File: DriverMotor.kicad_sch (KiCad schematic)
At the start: 15 parts, among them U3 DRV8874PWPR

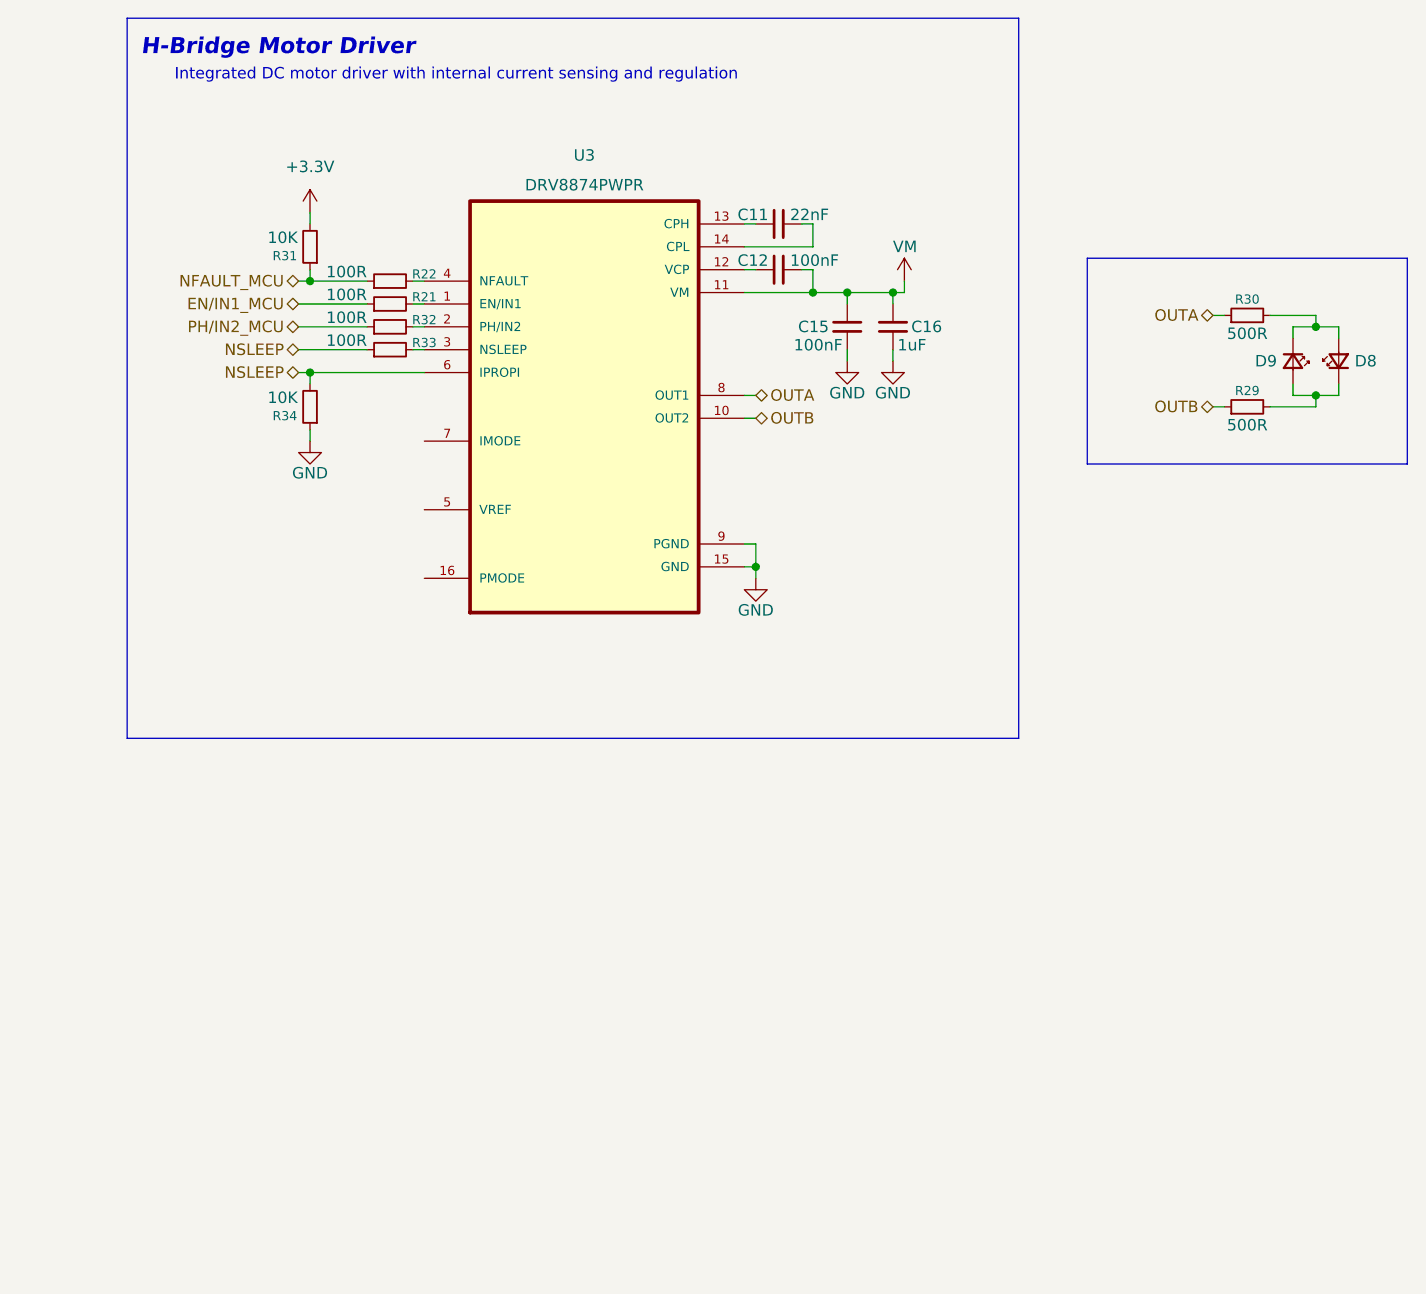
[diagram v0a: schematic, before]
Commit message: feat: integrate DRV8874 H-bridge stage with current sensing and polarity LEDs
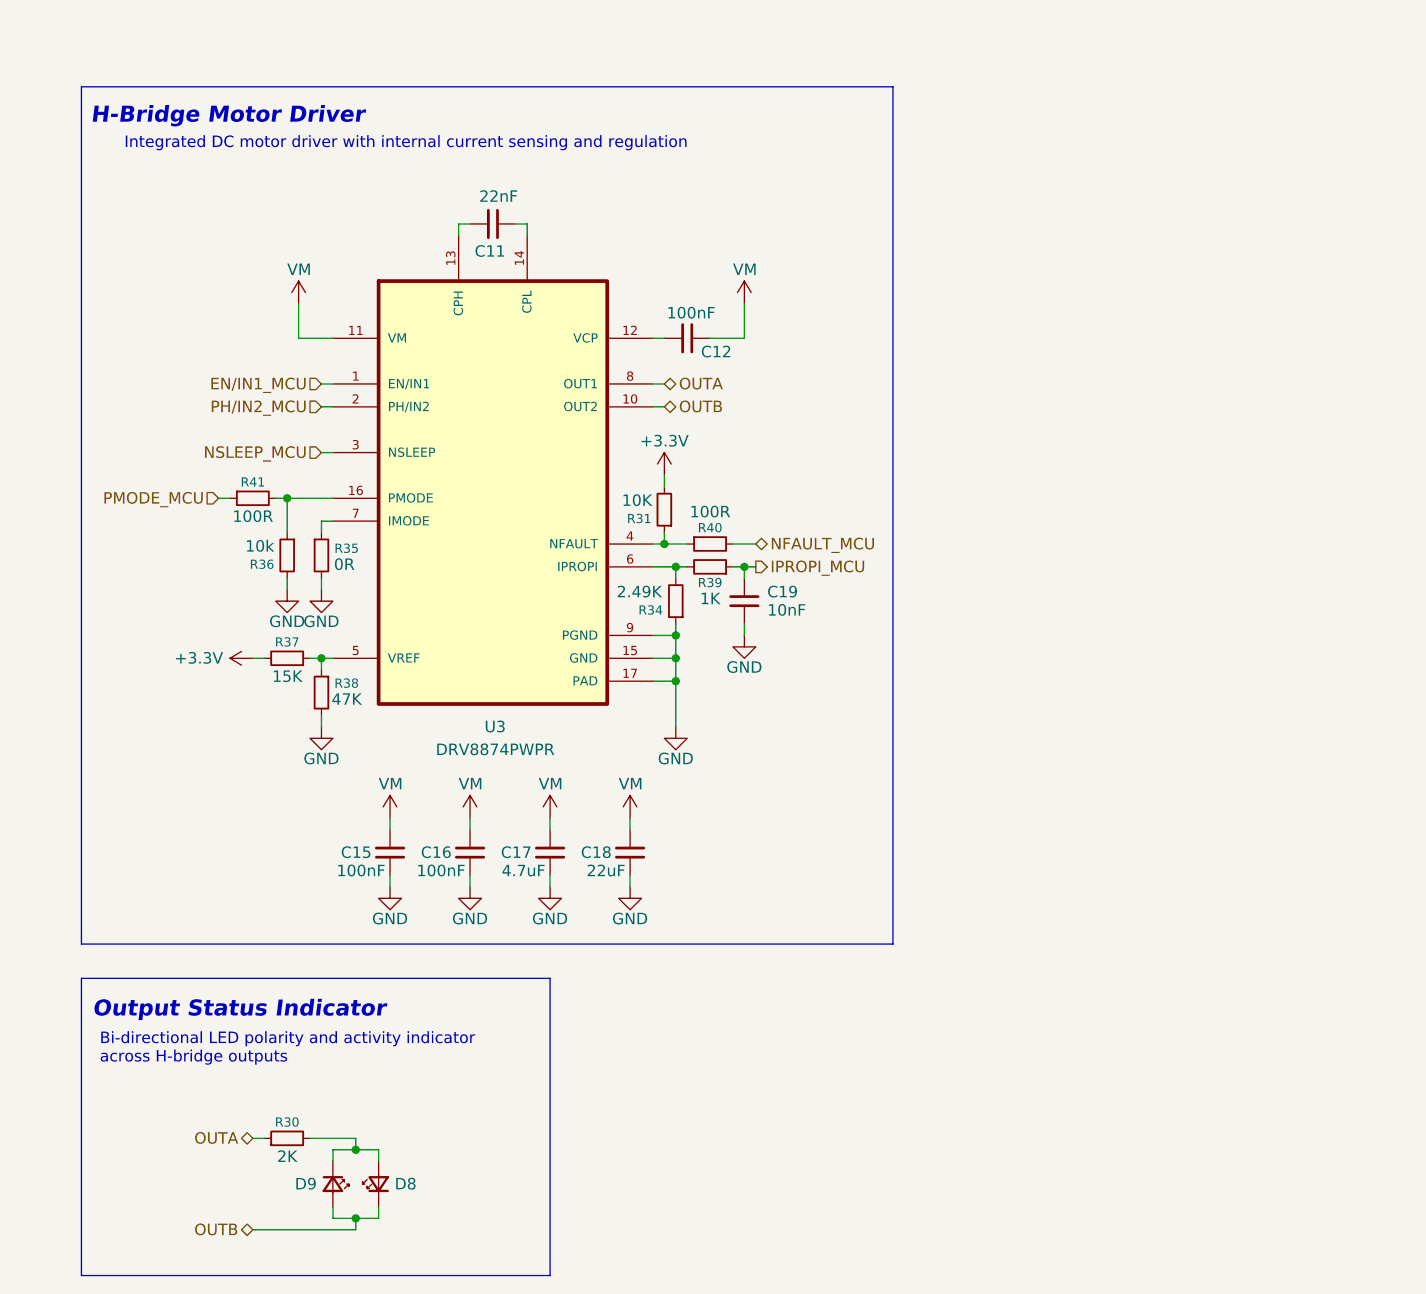
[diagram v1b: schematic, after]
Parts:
- removed R21, R22, R32, R33: 100R, Resistor_SMD:R_0603_1608Metric, symbol Device:R_Small
- removed R29: 500R, Resistor_SMD:R_0603_1608Metric, symbol Device:R_Small
- added C17: 4.7uF, Capacitor_SMD:C_0603_1608Metric, symbol Device:C_Small
- added C18: 22uF, Capacitor_SMD:C_0603_1608Metric, symbol Device:C_Small
- added C19: 10nF, Capacitor_SMD:C_0603_1608Metric, symbol Device:C_Small
- added R35: 0R, Resistor_SMD:R_0603_1608Metric, symbol Device:R_Small
- added R36: 10k, Resistor_SMD:R_0603_1608Metric, symbol Device:R_Small
- added R37: 15K, Resistor_SMD:R_0603_1608Metric, symbol Device:R_Small
- added R38: 47K, Resistor_SMD:R_0603_1608Metric, symbol Device:R_Small
- added R39: 1K, Resistor_SMD:R_0603_1608Metric, symbol Device:R_Small
- added R40, R41: 100R, Resistor_SMD:R_0603_1608Metric, symbol Device:R_Small
- C16: value 1uF -> 100nF
- R30: value 500R -> 2K
- R34: value 10K -> 2.49K
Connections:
- net +3.3V: now also R37.2
- net EN/IN1_MCU: now also U3.1 (EN/IN1)
- net GND: now also U3.17 (PAD), C17.2, C18.2, C19.1, R35.2, R36.2, R38.2
- net NFAULT_MCU: now also R40.2; no longer R31.1
- net OUTB: now also D8.1 (K), D9.2 (A)
- net PH/IN2_MCU: now also U3.2 (PH/IN2)
- net VM: now also C17.1, C18.1
- net at U3.16 (PMODE): now also R36.1, R41.2
- net NSLEEP_MCU: now reaches U3.3 (NSLEEP)
- net at U3.4 (NFAULT): now also R31.1, R40.1
- net at U3.5 (VREF): now also R37.1, R38.1
- net at U3.7 (IMODE): now also R35.1
- net NSLEEP: no longer names the net of R34.2, U3.6 (IPROPI)
- net NSLEEP: now also R39.2
- new net IPROPI_MCU: C19.2, R39.1
- new net PMODE_MCU: R41.1
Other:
- note added: "Bi-directional LED polarity and activity indicator across H-bridge outputs"
- note added: "Output Status Indicator"
- company: (none) -> BerryRocket
- title: (none) -> KinetiCoreDC - DriverMotorDC
- moved on the sheet: C15, D8, D9, R30, R31
